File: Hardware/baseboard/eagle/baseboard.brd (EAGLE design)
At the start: 108 x 112 mm, 195 parts, among them J1 MICROUSB-FEM, X1 JST-4POS-2X4POS, X1.2 TACH/LAP, X2.2 VRAILS+, X2.3 5V+SoC

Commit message: Final Layout
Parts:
- moved GUIDE1 34.0 mm to (74.3, 44.3)
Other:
- board text added: "!INT"
- board text added: "+"
- board text added: "-"
- board text added: "51"
- board text added: "52"
- board text added: "53"
- board text added: "54"
- board text added: "55"
- board text added: "56"
- board text added: "57"
- board text added: "58"
- board text added: "59"
- board text added: "5VDC"
- board text added: "62"
- board text added: "65"
- board text added: "66"
- board text added: "67"
- board text added: "68"
- board text added: "69"
- board text added: "MOTOR"
- board text added: "NTC"
- board text added: "OD1"
- board text added: "OD2"
- board text added: "SCL"
- board text added: "SDA"
- board text added: "TACH/LAP"

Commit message: updated schematic
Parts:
- removed GUIDE1: BREAK.GUIDE40MIL-BREAK, kitt.con:PAD40MIL.HOLEGUIDE
- removed REF1: EAGLE EDU LIMIT, kitt.refs:REF_EAGLE.EDULIMIT
- removed REF2: REF.LOGO.UASUA, kitt.refs:REF_LOGO_UASUA
- added A10:REF1: EAGLE EDU LIMIT, kitt.refs:REF_EAGLE.EDULIMIT
- added A10:REF2: REF.LOGO.UASUA, kitt.refs:REF_LOGO_UASUA
- A5:R6: value 100kR -> 100kR/1%
- renumbered A5:U$1 to A5:T1
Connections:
- net TOP.V+PWR renamed +24V
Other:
- board text added: "D.HOEGLINGER S1620567019"

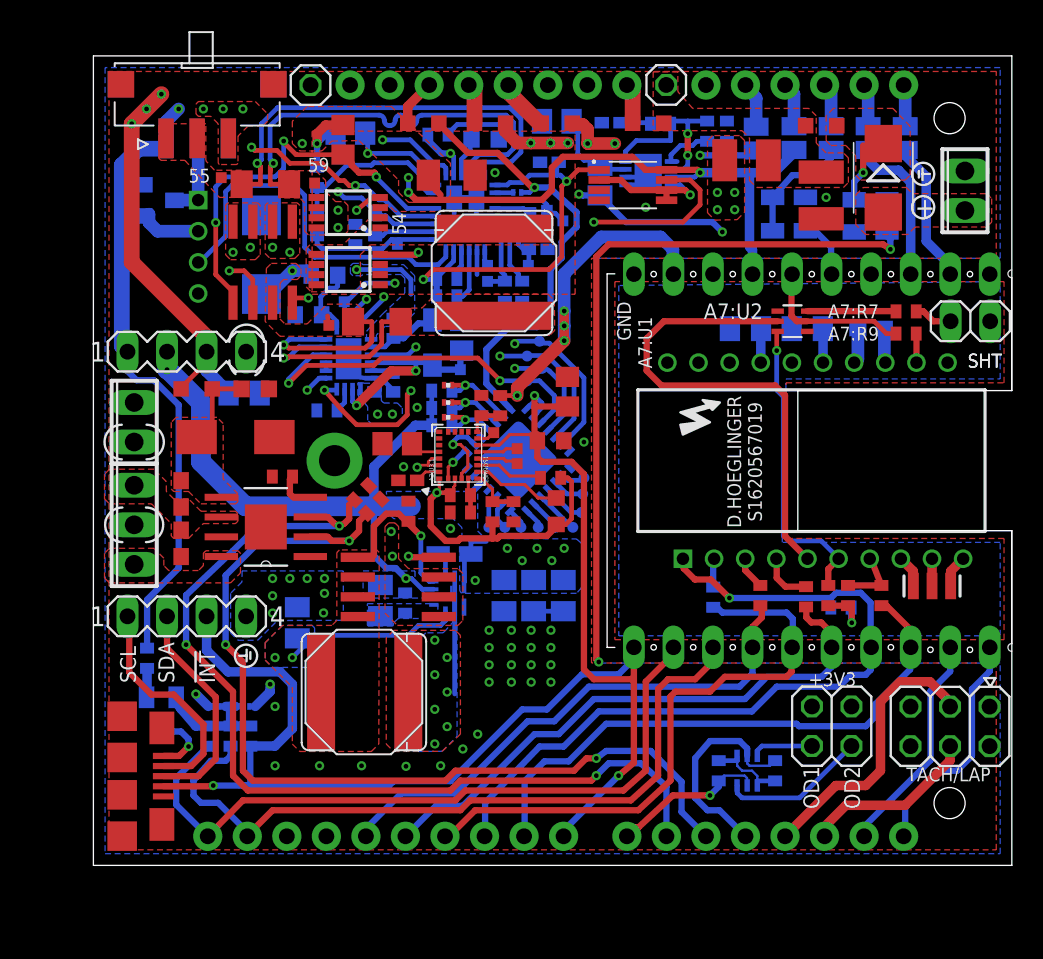
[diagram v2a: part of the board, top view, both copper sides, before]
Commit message: began fixing layout, inserted TODO at layer 118
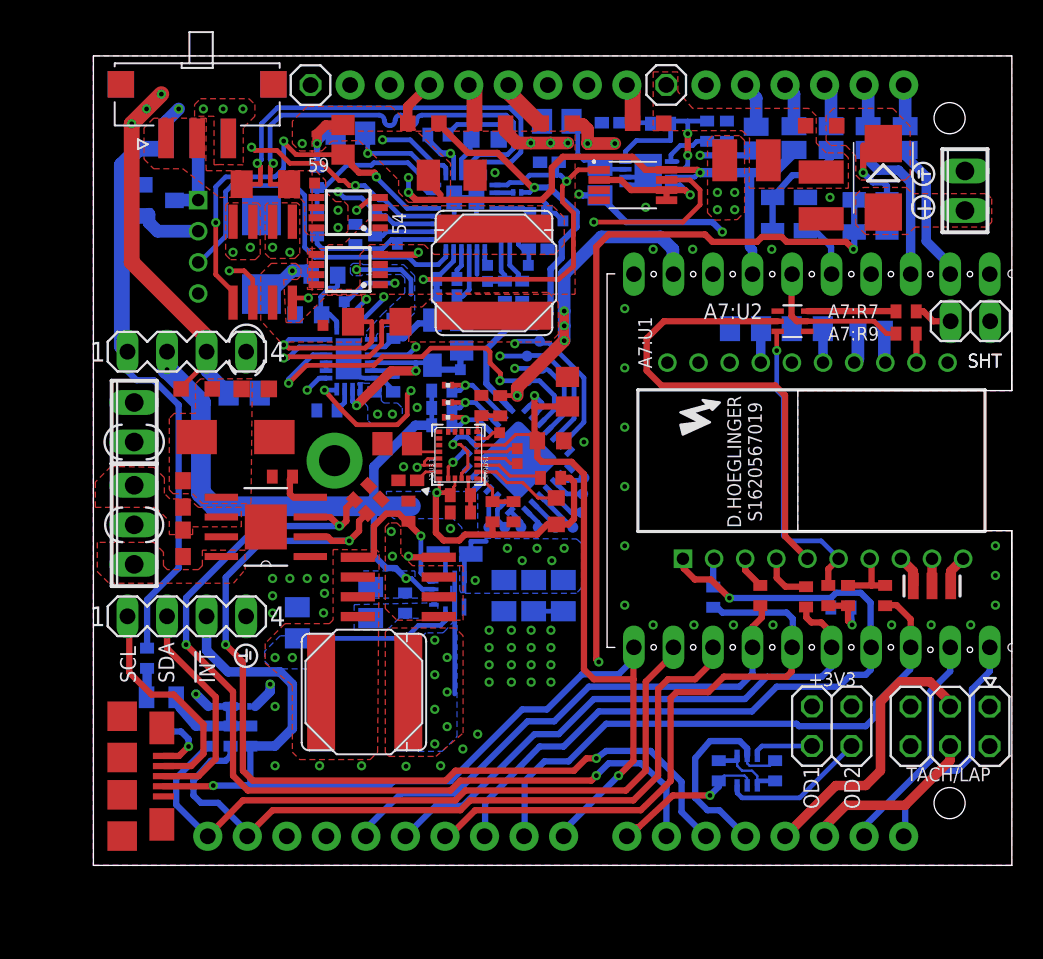
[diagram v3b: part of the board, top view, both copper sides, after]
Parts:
- removed A5:☇5: PTR1TP07SQ, testpad:TP07SQ
- moved A9:C5 0.64 mm to (22.8, 35.9)
- moved A3:☇3 0.38 mm to (31.1, 46.8)
- moved A6:☇3 0.38 mm to (19.7, 53.7)
- moved A7:R8 0.24 mm to (55.9, 36.3)
- moved A2:C4 0.12 mm to (10.8, 42.9)
- moved A2:C5 0.12 mm to (10.8, 39.7)
- turned A4:R1 to 180 degrees
- turned A4:R2 to 0 degrees
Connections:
- net VF+OUT/SWITCH: no longer A5:☇5.TP
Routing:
- net A2:VM: track 5.52 -> 1.22 mm
- net TOP.RRX: track 97.7 -> 95.0 mm
- net TOP.PWRON: track 27.5 -> 28.9 mm
- net TOP.RUN: track 24.2 -> 25.5 mm
- net +5V: track 89.6 -> 90.8 mm
- net +3V3: track 76.6 -> 75.7 mm
- net TOP.VSYS/GUARD: track 21.9 -> 21.0 mm
- net A4:N$1: track 4.94 -> 5.73 mm
- net TOP.OS1IS2: track 21.7 -> 21.1 mm
- net GND: vias 40 -> 59
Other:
- board text removed: "55"

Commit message: todo items should be fixed
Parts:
- moved A5:☇4 0.33 mm to (24.8, 59.0)
- moved A2:C2 0.32 mm to (15.7, 49.6)
- moved A5:R5 0.24 mm to (21.0, 65.8)
- moved A5:☇9 0.22 mm to (19.4, 63.0)
- moved A5:R7 0.16 mm to (21.8, 59.4)
- moved A3:☇1 0.16 mm to (32.4, 44.8)
- moved A3:☇2 0.16 mm to (32.4, 45.8)
- turned A2:L1 to 0 degrees
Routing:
- net GND: track 20.6 -> 27.5 mm
- net TOP.RUN: track 25.5 -> 23.8 mm
- net VDD: track 48.9 -> 47.2 mm
- net +3V3: track 75.7 -> 74.0 mm
- net +5V: track 90.8 -> 91.8 mm
- net +4.1V: track 105.3 -> 104.4 mm
- net A5:↔FBG: track 9.93 -> 9.24 mm
- net A5:CSN: track 26.6 -> 27.2 mm
- net +18V: track 38.2 -> 37.6 mm
- net TOP.!RST: track 67.4 -> 68.0 mm
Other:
- board text added: "TODO (Armin): ch bin soeben mit der Durchsicht deines Layouts fertig geworden. Beim näheren Betrachten sind mir noch folgende Dinge aufgefallen, die du bitte unbedingt beachten bzw. abändern solltest, * Einen aussagekräftigen Platinennamen inkl. Versionsnummer vergeben ("Baseboard-production" ist nämlich keiner ;-)..) z.B.: CarrerAI_....._V1.0 * Die Schriftzüge "Made in Austria" & "Copyright by H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"
- board text removed: "TODO ADD OPT. FB NETWORK BECAUSE LAYOUT"
- board text removed: "TODO: add an axis guide on silkscreen layer for gyro"
- board text removed: "[eq1]"
- board text removed: "conf"
